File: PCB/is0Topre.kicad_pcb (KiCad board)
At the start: 2 copper layers, 28.6 x 49.7 mm, 34 parts, among them Q1 2N7002, SW1 SW_Push, SW2 EC_SW, U1 ATmega32U4-M, U2 OPA350, Y1 16MHz

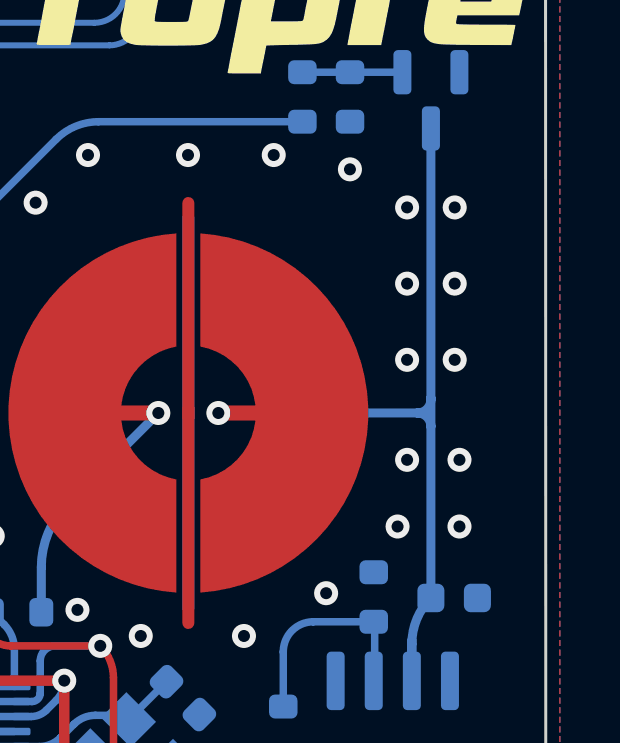
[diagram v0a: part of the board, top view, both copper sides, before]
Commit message: Fix for resistor missing
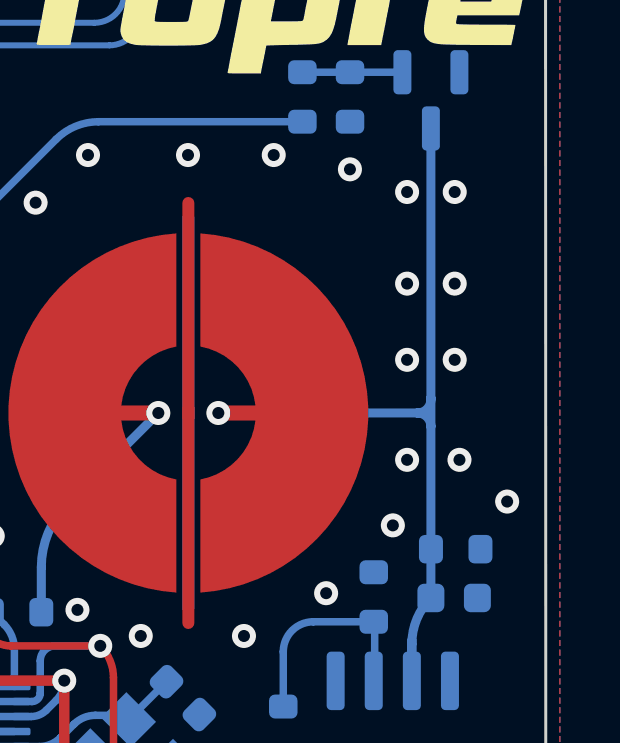
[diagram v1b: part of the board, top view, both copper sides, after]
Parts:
- added R12: 100k, Resistor_SMD:R_0603_1608Metric, B.Cu at (110.8, 66.0)
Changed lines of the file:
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@@
       (disableapertmacros false)
       (usegerberextensions false)
-      (usegerberattributes true)
-      (usegerberadvancedattributes true)
+      (usegerberattributes false)
+      (usegerberadvancedattributes false)
       (creategerberjobfile true)
       (svguseinch false)
@@
       (plotinvisibletext false)
       (sketchpadsonfab false)
-      (subtractmaskfromsilk false)
+      (subtractmaskfromsilk true)
       (outputformat 1)
       (mirror false)
-      (drillshape 1)
+      (drillshape 0)
       (scaleselection 1)
-      (outputdirectory "")
+      (outputdirectory "gerber-is0Topre")
     )
   )
@@
   (net 41 "ADC")
   (net 42 "unconnected-(U1-Pad11)")
-  (net 43 "Net-(U1-Pad12)")
+  (net 43 "Net-(R11-Pad2)")
   (net 44 "unconnected-(U1-Pad22)")
   (net 45 "unconnected-(U1-Pad25)")
@@
     (property "Sheetfile" "is0Topre.kicad_sch")
     (property "Sheetname" "")
-    (attr smd exclude_from_pos_files exclude_from_bom)
+    (attr smd exclude_from_pos_files)
     (fp_text reference "SW2" (at -6 -8) (layer "Dwgs.User")
       (effects (font (size 0.8 0.8) (thickness 0.12)))
@@
     (property "Sheetfile" "is0Topre.kicad_sch")
     (property "Sheetname" "")
-    (attr exclude_from_pos_files exclude_from_bom)
+    (attr exclude_from_pos_files)
     (fp_text reference "SW1" (at 0 2.65) (layer "Dwgs.User") hide
       (effects (font (size 1 1) (thickness 0.15)))
@@
     (property "Sheetname" "")
     (attr smd)
-    (fp_text reference "C8" (at 0.01875 -1.42875) (layer "B.SilkS")
+    (fp_text reference "C8" (at 1.607822 1.708199 90) (layer "B.SilkS")
       (effects (font (size 1 1) (thickness 0.15)) (justify mirror))
     )
@@
   )
   (footprint "Resistor_SMD:R_0603_1608Metric" (layer "B.Cu")
+    (at 110.83875 66.04 180)
+    (descr "Resistor SMD 0603 (1608 Metric), square (rectangular) end terminal, IPC_7351 nominal, (Body size source: IPC-SM-782 page 72, https://www.pcb-3d.com/wordpress/wp-content/uploads/ipc-sm-782a_amendment_1_and_2.pdf), generated with kicad-footprint-generator")
+    (tags "resistor")
+    (property "Sheetfile" "is0Topre.kicad_sch")
+    (property "Sheetname" "")
+    (attr smd)
+    (fp_text reference "R12" (at 0 1.43) (layer "B.SilkS")
+      (effects (font (size 1 1) (thickness 0.15)) (justify mirror))
+    )
+    (fp_text value "100k" (at 0 -1.43) (layer "B.Fab")
+      (effects (font (size 1 1) (thickness 0.15)) (justify mirror))
+    )
+    (fp_text user "${REFERENCE}" (at 0 0) (layer "B.Fab")
+      (effects (font (size 0.4 0.4) (thickness 0.06)) (justify mirror))
+    )
+    (fp_line (start -0.237258 0.5225) (end 0.237258 0.5225) (layer "B.SilkS") (width 0.12))
+    (fp_line (start -0.237258 -0.5225) (end 0.237258 -0.5225) (layer "B.SilkS") (width 0.12))
+    (fp_line (start 1.48 0.73) (end 1.48 -0.73) (layer "B.CrtYd") (width 0.05))
+    (fp_line (start -1.48 -0.73) (end -1.48 0.73) (layer "B.CrtYd") (width 0.05))
+    (fp_line (start 1.48 -0.73) (end -1.48 -0.73) (layer "B.CrtYd") (width 0.05))
+    (fp_line (start -1.48 0.73) (end 1.48 0.73) (layer "B.CrtYd") (width 0.05))
+    (fp_line (start -0.8 0.4125) (end 0.8 0.4125) (layer "B.Fab") (width 0.1))
+    (fp_line (start 0.8 0.4125) (end 0.8 -0.4125) (layer "B.Fab") (width 0.1))
+    (fp_line (start 0.8 -0.4125) (end -0.8 -0.4125) (layer "B.Fab") (width 0.1))
+    (fp_line (start -0.8 -0.4125) (end -0.8 0.4125) (layer "B.Fab") (width 0.1))
+    (pad "1" smd roundrect (at -0.825 0 180) (size 0.8 0.95) (layers "B.Cu" "B.Paste" "B.Mask") (roundrect_rratio 0.25)
+      (net 2 "GND") (pintype "passive"))
+    (pad "2" smd roundrect (at 0.825 0 180) (size 0.8 0.95) (layers "B.Cu" "B.Paste" "B.Mask") (roundrect_rratio 0.25)
+      (net 34 "ROW0") (pintype "passive"))
+    (model "${KICAD6_3DMODEL_DIR}/Resistor_SMD.3dshapes/R_0603_1608Metric.wrl"
+      (offset (xyz 0 0 0))
+      (scale (xyz 1 1 1))
+      (rotate (xyz 0 0 0))
+    )
+  )
+  (footprint "Resistor_SMD:R_0603_1608Metric" (layer "B.Cu")
     (at 102.438428 46.667427)
     (descr "Resistor SMD 0603 (1608 Metric), square (rectangular) end terminal, IPC_7351 nominal, (Body size source: IPC-SM-782 page 72, https://www.pcb-3d.com/wordpress/wp-content/uploads/ipc-sm-782a_amendment_1_and_2.pdf), generated with kicad-footprint-generator")
@@
     (property "Sheetname" "")
     (attr smd)
-    (fp_text reference "Q1" (at 3.09375 0.9525 -270) (layer "B.SilkS")
+    (fp_text reference "Q1" (at -2.818051 1.109678 -270) (layer "B.SilkS")
       (effects (font (size 1 1) (thickness 0.15)) (justify mirror))
     )
@@
       (net 42 "unconnected-(U1-Pad11)") (pinfunction "PB3") (pintype "bidirectional+no_connect"))
     (pad "12" smd roundrect (at -2.5 -3.3375 270) (size 0.25 1.075) (layers "B.Cu" "B.Paste" "B.Mask") (roundrect_rratio 0.25)
-      (net 43 "Net-(U1-Pad12)") (pinfunction "PB7") (pintype "bidirectional"))
+      (net 43 "Net-(R11-Pad2)") (pinfunction "PB7") (pintype "bidirectional"))
     (pad "13" smd roundrect (at -2 -3.3375 270) (size 0.25 1.075) (layers "B.Cu" "B.Paste" "B.Mask") (roundrect_rratio 0.25)
       (net 9 "RST") (pinfunction "~{RESET}") (pintype "input"))
@@
       (net 35 "COL0") (pintype "passive"))
     (pad "2" smd roundrect (at 0.825 0 180) (size 0.8 0.95) (layers "B.Cu" "B.Paste" "B.Mask") (roundrect_rratio 0.25)
-      (net 43 "Net-(U1-Pad12)") (pintype "passive"))
+      (net 43 "Net-(R11-Pad2)") (pintype "passive"))
     (model "${KICAD6_3DMODEL_DIR}/Resistor_SMD.3dshapes/R_0603_1608Metric.step"
       (offset (xyz 0 0 0))
@@
   (via (at 93.880928 67.223051) (size 0.8) (drill 0.4) (layers "F.Cu" "B.Cu") (free) (net 2))
   (via (at 101.598428 81.318051) (size 0.8) (drill 0.4) (layers "F.Cu" "B.Cu") (free) (net 2))
-  (via (at 109.218428 54.648051) (size 0.8) (drill 0.4) (layers "F.Cu" "B.Cu") (free) (net 2))
+  (via (at 109.218428 54.13375) (size 0.8) (drill 0.4) (layers "F.Cu" "B.Cu") (free) (net 2))
   (via (at 103.210928 76.173051) (size 0.8) (drill 0.4) (layers "F.Cu" "B.Cu") (free) (net 2))
-  (via (at 108.900928 65.284301) (size 0.8) (drill 0.4) (layers "F.Cu" "B.Cu") (free) (net 2))
+  (via (at 108.74375 65.24625) (size 0.8) (drill 0.4) (layers "F.Cu" "B.Cu") (free) (net 2))
   (via (at 104.773428 52.901801) (size 0.8) (drill 0.4) (layers "F.Cu" "B.Cu") (free) (net 2))
   (via (at 100.340928 68.933051) (size 0.8) (drill 0.4) (layers "F.Cu" "B.Cu") (free) (net 2))
   (via (at 92.775928 73.133051) (size 0.8) (drill 0.4) (layers "F.Cu" "B.Cu") (net 2))
-  (via (at 110.964678 65.284301) (size 0.8) (drill 0.4) (layers "F.Cu" "B.Cu") (free) (net 2))
+  (via (at 112.55375 64.4525) (size 0.8) (drill 0.4) (layers "F.Cu" "B.Cu") (free) (net 2))
   (via (at 109.218428 57.188051) (size 0.8) (drill 0.4) (layers "F.Cu" "B.Cu") (free) (net 2))
-  (via (at 110.805928 54.648051) (size 0.8) (drill 0.4) (layers "F.Cu" "B.Cu") (free) (net 2))
+  (via (at 110.805928 54.13375) (size 0.8) (drill 0.4) (layers "F.Cu" "B.Cu") (free) (net 2))
   (via (at 110.647178 72.904301) (size 0.8) (drill 0.4) (layers "F.Cu" "B.Cu") (free) (net 2))
   (via (at 90.485928 64.649301) (size 0.8) (drill 0.4) (layers "F.Cu" "B.Cu") (free) (net 2))

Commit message: Update of circuit after PCB testing
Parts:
- removed the G*** at (110.0, 45.0)
- removed Q1: 2N7002, Package_TO_SOT_SMD:SOT-23
- removed the R7 at (105.7, 51.0)
- removed the R8 at (107.3, 51.0)
- added D2: SK6812MINI, LED_SMD:LED_SK6812MINI_PLCC4_3.5x3.5mm_P1.75mm, B.Cu at (99.5, 51.9)
- R8: renamed from R10; value 47k -> 100k
- renumbered R9 to R7
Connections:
- C8 pad 1: ROW0 -> DISCHARGE_PIN
- R12 pad 2: ROW0 -> DISCHARGE_PIN
- SW2 pad 2: ROW0 -> DISCHARGE_PIN
- U1 pad 39: unconnected-(U1-Pad39) -> LED
- U2 pad 3: ROW0 -> DISCHARGE_PIN
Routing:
- net DISCHARGE_PIN: track 36.3 -> 71.5 mm, vias 2 -> 3
- net LED: track 0.00 -> 30.9 mm, vias 0 -> 2
- net ROW0: track 28.0 -> 0.00 mm, vias 1 -> 0
- net VCC: track 94.7 -> 105.9 mm, vias 6 -> 8
- net Net-(Q1-Pad1): track 3.33 -> 0.00 mm
- net GND: vias 68 -> 67
